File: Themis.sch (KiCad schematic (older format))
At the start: 47 parts, among them J1 SMA, J10 Conn_01x01, J11 Conn_01x01, J12 Conn_01x01, J13 Conn_01x01, J14 SMA, J15 SMA, J16 SMA, J17 SMA, J18 Conn_01x01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

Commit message: Branch for Themis V1
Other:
- note added: "Themis V1\npremière version du coupleur\npcb réalisé, tests peu concluants\n"
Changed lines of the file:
@@
 EESchema Schematic File Version 2
+LIBS:ee2-5nu
+LIBS:Amplifier_Operational
+LIBS:Connector_Generic
+LIBS:Device
 LIBS:power
-LIBS:device
-LIBS:relays
-LIBS:conn
-LIBS:linear
-LIBS:ee2-5nu
+LIBS:Regulator_Linear
 LIBS:Themis-cache
 EELAYER 25 0
@@
 Text Notes 3950 3650 2    60   ~ 0
 PS\nFeedback\n
+Text Notes 2400 1350 0    60   ~ 0
+Themis V1\npremière version du coupleur\npcb réalisé, tests peu concluants\n
 $EndSCHEMATC

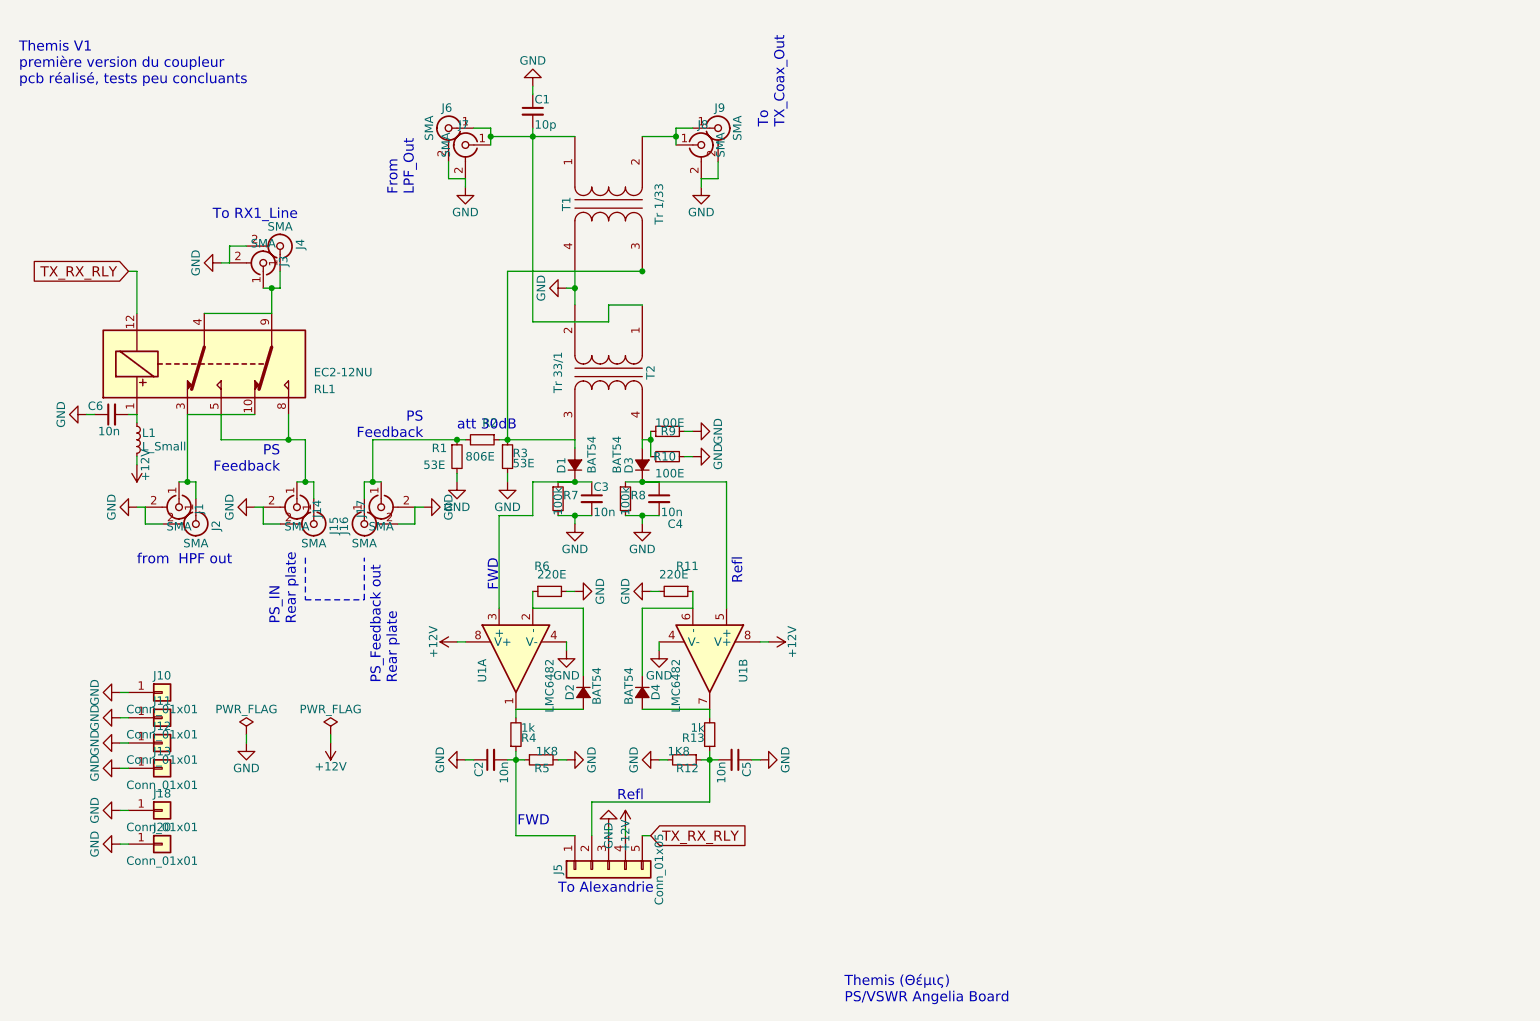
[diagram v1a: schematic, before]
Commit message: simplified version, no relay
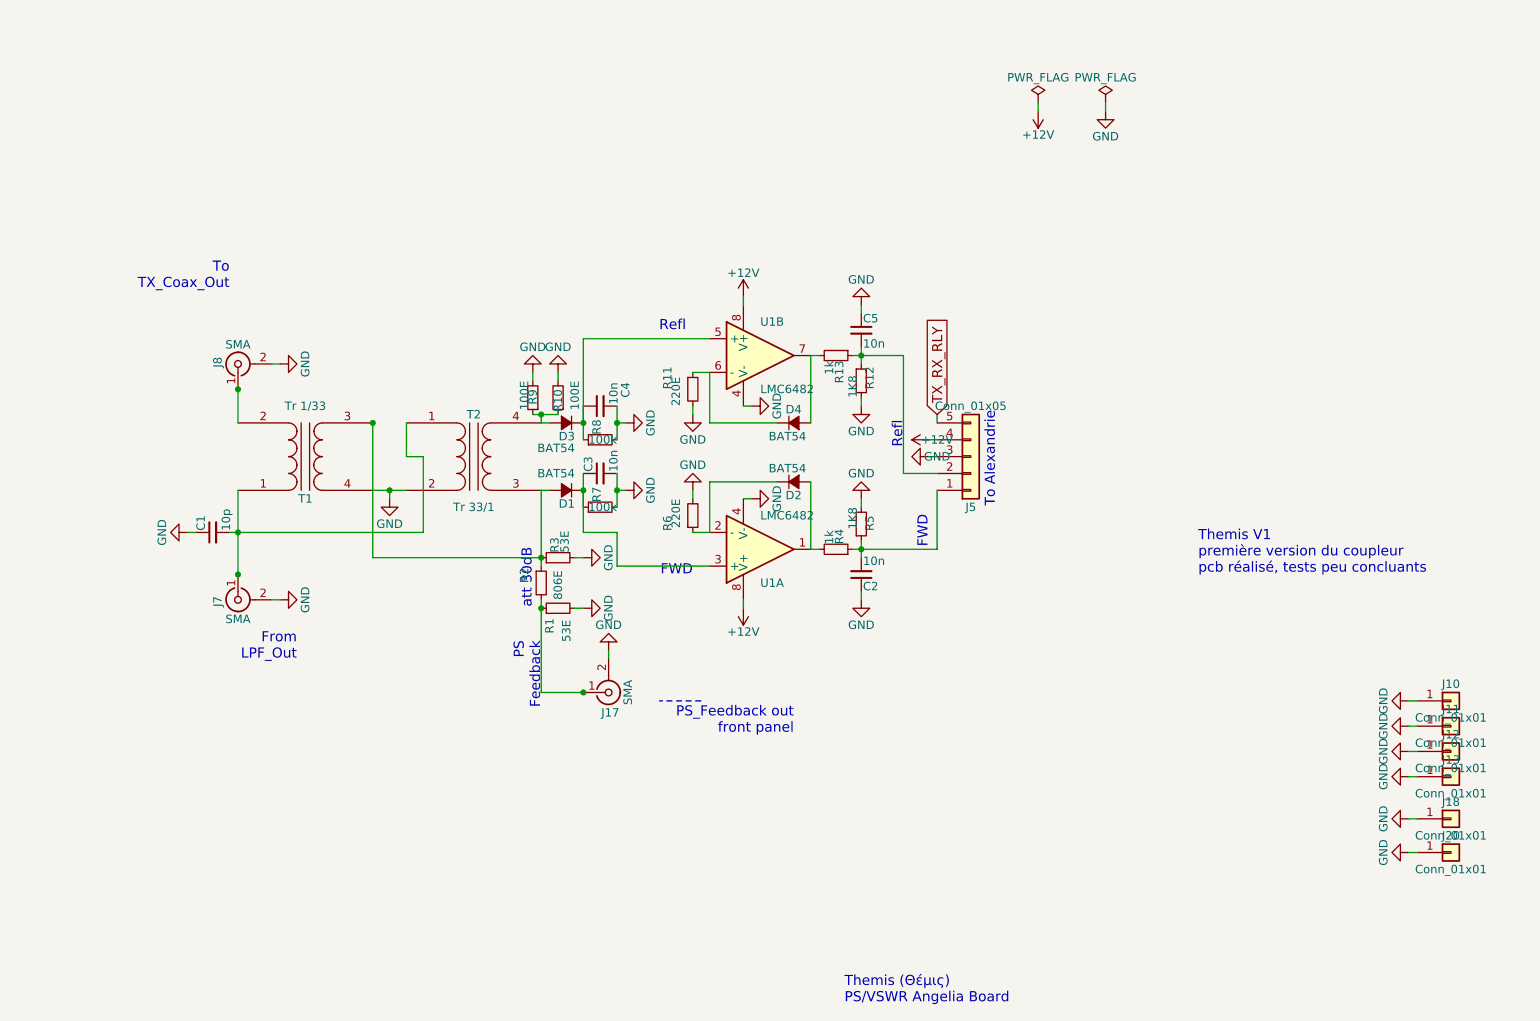
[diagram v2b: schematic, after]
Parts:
- removed C6: 10n, Capacitors_SMD:C_0805_HandSoldering, symbol C_Small
- removed J1, J14, J3, J6: SMA, SMA_PINS:SMA_EDGE_NRW, symbol Conn_Coaxial
- removed J15, J16, J2, J4, J9: SMA, SMA_PINS:SMA_PINS, symbol Conn_Coaxial
- removed L1: L_Small, Inductors_SMD:L_0805_HandSoldering, symbol L_Small
- removed RL1: EC2-12NU, 2_Form_C_Relay:Relay_DPDT_NEC_EC2, symbol EC2-12NU
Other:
- note added: "PS_Feedback out\nfront panel\n"
- note removed: "PS_Feedback out\nRear plate"
- note removed: "PS_IN\nRear plate"
- note removed: "To RX1_Line"
- note removed: "from HPF out"
- moved on the sheet: C1, C2, C3, C4, C5, D1, D2, D3, D4, J10, J11, J12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
